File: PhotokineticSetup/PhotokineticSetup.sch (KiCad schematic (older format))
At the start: 28 parts, among them J1 Conn_01x02, J2 Serial, J3 LEDs, J4 Switches, J5 Outputs, J6 Inputs, J7 Conn_01x20, J8 Conn_01x20, Q1 2N3904, Q2 2N3904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

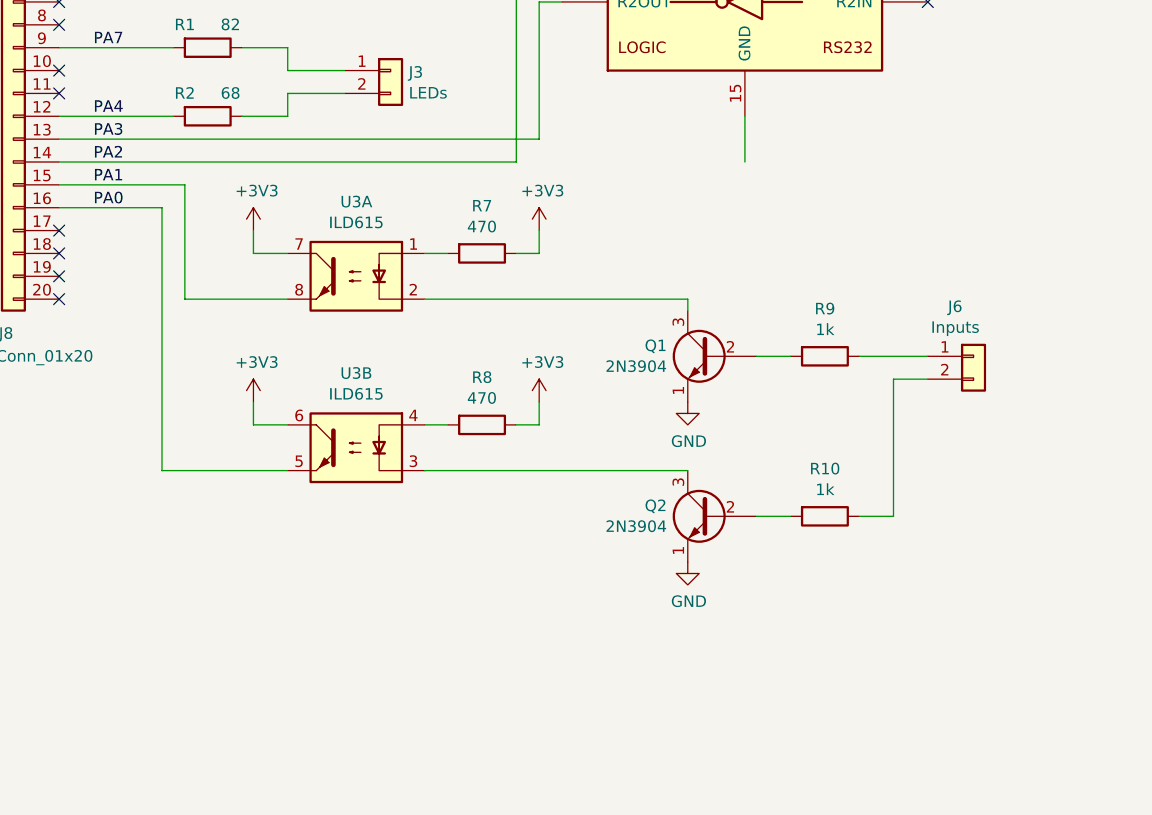
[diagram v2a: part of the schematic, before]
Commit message: Missing GND node + better placement of R7 & R8
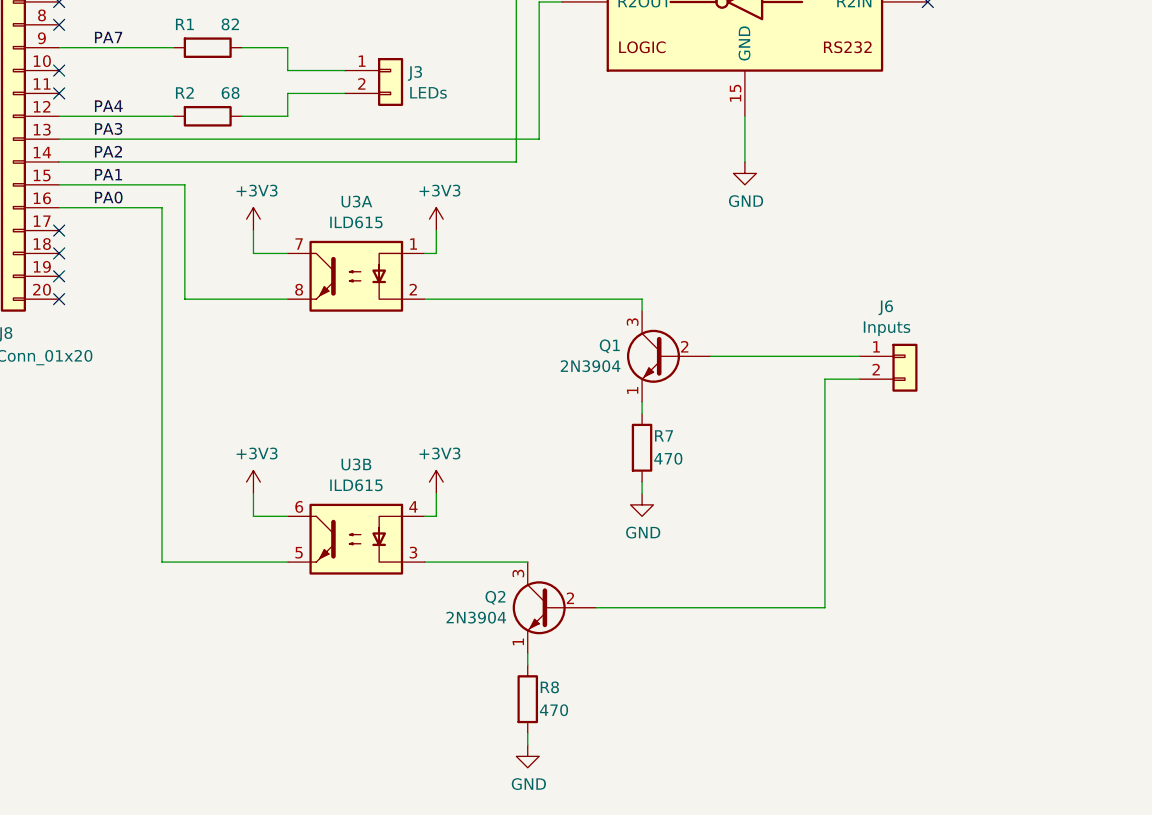
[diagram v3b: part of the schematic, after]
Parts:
- removed R10, R9: 1k, Resistor_THT:R_Axial_DIN0204_L3.6mm_D1.6mm_P7.62mm_Horizontal, symbol Device:R
- renumbered R8 to R7, R7 to R8
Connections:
- net +3V3: now also U3.1, U3.4; no longer R7.1, R8.1
- net GND: now also R7.2, R8.2, U1.15 (GND); no longer Q1.1 (E), Q2.1 (E)
- net at J6.1 (Pin_1): now also Q1.2 (B)
- net at J6.2 (Pin_2): now also Q2.2 (B)
- new net: Q1.1 (E), R7.1
- new net: Q2.1 (E), R8.1
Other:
- moved on the sheet: J6, Q1, Q2, R7, R8, U3B
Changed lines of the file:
@@
 	8250 4150 8250 4350
-$Comp
-L power:GND #PWR0104
-U 1 1 60C4DEDC
-P 8000 5400
-F 0 "#PWR0104" H 8000 5150 50  0001 C CNN
-F 1 "GND" H 8005 5227 50  0000 C CNN
-F 2 "" H 8000 5400 50  0001 C CNN
-F 3 "" H 8000 5400 50  0001 C CNN
-	1    8000 5400
-	1    0    0    -1
-$EndComp
 $Comp
 L power:+5V #PWR0105
@@
 L Connector_Generic:Conn_01x02 J6
 U 1 1 60C97537
-P 9250 5200
-F 0 "J6" H 9170 5417 50  0000 C CNN
-F 1 "Inputs" H 9170 5326 50  0000 C CNN
-F 2 "Connector_PinHeader_2.54mm:PinHeader_1x02_P2.54mm_Vertical" H 9250 5200 50  0001 C CNN
-F 3 "~" H 9250 5200 50  0001 C CNN
-	1    9250 5200
+P 8950 5200
+F 0 "J6" H 8870 5417 50  0000 C CNN
+F 1 "Inputs" H 8870 5326 50  0000 C CNN
+F 2 "Connector_PinHeader_2.54mm:PinHeader_1x02_P2.54mm_Vertical" H 8950 5200 50  0001 C CNN
+F 3 "~" H 8950 5200 50  0001 C CNN
+	1    8950 5200
 	1    0    0    -1
 $EndComp
@@
 L Isolator:ILD74 U3
 U 2 1 60CA65A1
-P 6550 5600
-F 0 "U3" H 6550 5925 50  0000 C CNN
-F 1 "ILD615" H 6550 5834 50  0000 C CNN
-F 2 "Package_DIP:DIP-8_W7.62mm_Socket_LongPads" H 6350 5400 50  0001 L CIN
-F 3 "https://www.vishay.com/docs/83640/ild74.pdf" H 6550 5600 50  0001 L CNN
-	2    6550 5600
-	-1   0    0    -1
+P 6550 6000
+F 0 "U3" H 6550 6325 50  0000 C CNN
+F 1 "ILD615" H 6550 6234 50  0000 C CNN
+F 2 "Package_DIP:DIP-8_W7.62mm_Socket_LongPads" H 6350 5800 50  0001 L CIN
+F 3 "https://www.vishay.com/docs/83640/ild74.pdf" H 6550 6000 50  0001 L CNN
+	2    6550 6000
+	-1   0    0    -1
+$EndComp
+$Comp
+L Device:R R8
+U 1 1 60CA929B
+P 7300 6700
+F 0 "R8" H 7350 6750 50  0000 L CNN
+F 1 "470" H 7350 6650 50  0000 L CNN
+F 2 "Resistor_THT:R_Axial_DIN0204_L3.6mm_D1.6mm_P7.62mm_Horizontal" V 7230 6700 50  0001 C CNN
+F 3 "~" H 7300 6700 50  0001 C CNN
+	1    7300 6700
+	1    0    0    -1
 $EndComp
 $Comp
 L Device:R R7
-U 1 1 60CA929B
-P 7100 4750
-F 0 "R7" V 6893 4750 50  0000 C CNN
-F 1 "470" V 6984 4750 50  0000 C CNN
-F 2 "Resistor_THT:R_Axial_DIN0204_L3.6mm_D1.6mm_P7.62mm_Horizontal" V 7030 4750 50  0001 C CNN
-F 3 "~" H 7100 4750 50  0001 C CNN
-	1    7100 4750
-	0    1    1    0
-$EndComp
-$Comp
-L Device:R R8
 U 1 1 60CA92A2
-P 7100 5500
-F 0 "R8" V 6893 5500 50  0000 C CNN
-F 1 "470" V 6984 5500 50  0000 C CNN
-F 2 "Resistor_THT:R_Axial_DIN0204_L3.6mm_D1.6mm_P7.62mm_Horizontal" V 7030 5500 50  0001 C CNN
-F 3 "~" H 7100 5500 50  0001 C CNN
-	1    7100 5500
-	0    1    1    0
+P 7800 5600
+F 0 "R7" H 7850 5650 50  0000 L CNN
+F 1 "470" H 7850 5550 50  0000 L CNN
+F 2 "Resistor_THT:R_Axial_DIN0204_L3.6mm_D1.6mm_P7.62mm_Horizontal" V 7730 5600 50  0001 C CNN
+F 3 "~" H 7800 5600 50  0001 C CNN
+	1    7800 5600
+	1    0    0    -1
 $EndComp
 $Sheet
@@
 L Transistor_BJT:2N3904 Q1
 U 1 1 60CA79CE
-P 8100 5200
-F 0 "Q1" H 8291 5246 50  0000 L CNN
-F 1 "2N3904" H 8291 5155 50  0000 L CNN
-F 2 "Package_TO_SOT_THT:TO-92_Inline" H 8300 5125 50  0001 L CIN
-F 3 "https://www.fairchildsemi.com/datasheets/2N/2N3904.pdf" H 8100 5200 50  0001 L CNN
-	1    8100 5200
-	-1   0    0    -1
-$EndComp
-Wire Wire Line
-	7250 4750 7350 4750
-Wire Wire Line
-	7250 5500 7350 5500
+P 7900 5200
+F 0 "Q1" H 8091 5246 50  0000 L CNN
+F 1 "2N3904" H 8091 5155 50  0000 L CNN
+F 2 "Package_TO_SOT_THT:TO-92_Inline" H 8100 5125 50  0001 L CIN
+F 3 "https://www.fairchildsemi.com/datasheets/2N/2N3904.pdf" H 7900 5200 50  0001 L CNN
+	1    7900 5200
+	-1   0    0    -1
+$EndComp
 $Comp
 L power:+3V3 #PWR0113
 U 1 1 60CFEBE2
-P 7350 4650
-F 0 "#PWR0113" H 7350 4500 50  0001 C CNN
-F 1 "+3V3" H 7365 4823 50  0000 C CNN
-F 2 "" H 7350 4650 50  0001 C CNN
-F 3 "" H 7350 4650 50  0001 C CNN
-	1    7350 4650
-	1    0    0    -1
-$EndComp
-Wire Wire Line
-	7350 4650 7350 4750
+P 6900 4650
+F 0 "#PWR0113" H 6900 4500 50  0001 C CNN
+F 1 "+3V3" H 6915 4823 50  0000 C CNN
+F 2 "" H 6900 4650 50  0001 C CNN
+F 3 "" H 6900 4650 50  0001 C CNN
+	1    6900 4650
+	1    0    0    -1
+$EndComp
+Wire Wire Line
+	6900 4650 6900 4750
 $Comp
 L power:+3V3 #PWR0114
 U 1 1 60D3CEA5
-P 7350 5400
-F 0 "#PWR0114" H 7350 5250 50  0001 C CNN
-F 1 "+3V3" H 7365 5573 50  0000 C CNN
-F 2 "" H 7350 5400 50  0001 C CNN
-F 3 "" H 7350 5400 50  0001 C CNN
-	1    7350 5400
-	1    0    0    -1
-$EndComp
-Wire Wire Line
-	7350 5400 7350 5500
-Wire Wire Line
-	6850 4750 6950 4750
-Wire Wire Line
-	6850 5500 6950 5500
-Wire Wire Line
-	8000 4950 8000 5000
-Wire Wire Line
-	6850 4950 8000 4950
+P 6900 5800
+F 0 "#PWR0114" H 6900 5650 50  0001 C CNN
+F 1 "+3V3" H 6915 5973 50  0000 C CNN
+F 2 "" H 6900 5800 50  0001 C CNN
+F 3 "" H 6900 5800 50  0001 C CNN
+	1    6900 5800
+	1    0    0    -1
+$EndComp
+Wire Wire Line
+	6900 5800 6900 5900
+Wire Wire Line
+	6850 4750 6900 4750
+Wire Wire Line
+	6850 5900 6900 5900
+Wire Wire Line
+	7800 4950 7800 5000
 $Comp
 L power:GND #PWR0115
 U 1 1 60D5D869
-P 8000 6100
-F 0 "#PWR0115" H 8000 5850 50  0001 C CNN
-F 1 "GND" H 8005 5927 50  0000 C CNN
-F 2 "" H 8000 6100 50  0001 C CNN
-F 3 "" H 8000 6100 50  0001 C CNN
-	1    8000 6100
+P 7300 6900
+F 0 "#PWR0115" H 7300 6650 50  0001 C CNN
+F 1 "GND" H 7305 6727 50  0000 C CNN
+F 2 "" H 7300 6900 50  0001 C CNN
+F 3 "" H 7300 6900 50  0001 C CNN
+	1    7300 6900
 	1    0    0    -1
 $EndComp
@@
 L Transistor_BJT:2N3904 Q2
 U 1 1 60D5D86F
-P 8100 5900
-F 0 "Q2" H 8291 5946 50  0000 L CNN
-F 1 "2N3904" H 8291 5855 50  0000 L CNN
-F 2 "Package_TO_SOT_THT:TO-92_Inline" H 8300 5825 50  0001 L CIN
-F 3 "https://www.fairchildsemi.com/datasheets/2N/2N3904.pdf" H 8100 5900 50  0001 L CNN
-	1    8100 5900
-	-1   0    0    -1
-$EndComp
-Wire Wire Line
-	6850 5700 8000 5700
+P 7400 6300
+F 0 "Q2" H 7591 6346 50  0000 L CNN
+F 1 "2N3904" H 7591 6255 50  0000 L CNN
+F 2 "Package_TO_SOT_THT:TO-92_Inline" H 7600 6225 50  0001 L CIN
+F 3 "https://www.fairchildsemi.com/datasheets/2N/2N3904.pdf" H 7400 6300 50  0001 L CNN
+	1    7400 6300
+	-1   0    0    -1
+$EndComp
 Wire Wire Line
 	1250 4550 1500 4550
@@
 Wire Wire Line
 	1800 4750 1950 4750
-$Comp
-L Device:R R10
-U 1 1 60CA7C5E
-P 8600 5900
-F 0 "R10" V 8393 5900 50  0000 C CNN
-F 1 "1k" V 8484 5900 50  0000 C CNN
-F 2 "Resistor_THT:R_Axial_DIN0204_L3.6mm_D1.6mm_P7.62mm_Horizontal" V 8530 5900 50  0001 C CNN
-F 3 "~" H 8600 5900 50  0001 C CNN
-	1    8600 5900
-	0    1    1    0
-$EndComp
-Wire Wire Line
-	8900 5900 8900 5300
-Wire Wire Line
-	8900 5300 9050 5300
-Wire Wire Line
-	8300 5900 8450 5900
-Wire Wire Line
-	8750 5900 8900 5900
-$Comp
-L Device:R R9
-U 1 1 60CC280A
-P 8600 5200
-F 0 "R9" V 8393 5200 50  0000 C CNN
-F 1 "1k" V 8484 5200 50  0000 C CNN
-F 2 "Resistor_THT:R_Axial_DIN0204_L3.6mm_D1.6mm_P7.62mm_Horizontal" V 8530 5200 50  0001 C CNN
-F 3 "~" H 8600 5200 50  0001 C CNN
-	1    8600 5200
-	0    1    1    0
-$EndComp
-Wire Wire Line
-	8750 5200 9050 5200
-Wire Wire Line
-	8300 5200 8450 5200
+Wire Wire Line
+	8600 5300 8750 5300
 Wire Wire Line
 	5800 4950 6250 4950
 Wire Wire Line
-	5700 5700 6250 5700
-Wire Wire Line
-	5700 4550 5700 5700
+	5700 6100 6250 6100
 Wire Wire Line
 	5800 4450 5800 4950
@@
 L power:+3V3 #PWR?
 U 1 1 60CBE08A
-P 6100 5400
-F 0 "#PWR?" H 6100 5250 50  0001 C CNN
-F 1 "+3V3" H 6115 5573 50  0000 C CNN
-F 2 "" H 6100 5400 50  0001 C CNN
-F 3 "" H 6100 5400 50  0001 C CNN
-	1    6100 5400
-	1    0    0    -1
-$EndComp
-Wire Wire Line
-	6100 5400 6100 5500
-Wire Wire Line
-	6100 5500 6250 5500
+P 6100 5800
+F 0 "#PWR?" H 6100 5650 50  0001 C CNN
+F 1 "+3V3" H 6115 5973 50  0000 C CNN
+F 2 "" H 6100 5800 50  0001 C CNN
+F 3 "" H 6100 5800 50  0001 C CNN
+	1    6100 5800
+	1    0    0    -1
+$EndComp
+Wire Wire Line
+	6100 5800 6100 5900
+Wire Wire Line
+	6100 5900 6250 5900
+$Comp
+L power:GND #PWR?
+U 1 1 60D05AB9
+P 8250 4350
+F 0 "#PWR?" H 8250 4100 50  0001 C CNN
+F 1 "GND" H 8255 4177 50  0000 C CNN
+F 2 "" H 8250 4350 50  0001 C CNN
+F 3 "" H 8250 4350 50  0001 C CNN
+	1    8250 4350
+	1    0    0    -1
+$EndComp
+Wire Wire Line
+	5700 4550 5700 6100
+Wire Wire Line
+	8100 5200 8750 5200
+Wire Wire Line
+	7600 6300 8600 6300
+$Comp
+L power:GND #PWR?
+U 1 1 60D74D00
+P 7800 5800
+F 0 "#PWR?" H 7800 5550 50  0001 C CNN
+F 1 "GND" H 7805 5627 50  0000 C CNN
+F 2 "" H 7800 5800 50  0001 C CNN
+F 3 "" H 7800 5800 50  0001 C CNN
+	1    7800 5800
+	1    0    0    -1
+$EndComp
+Wire Wire Line
+	7800 5750 7800 5800
+Wire Wire Line
+	7800 5400 7800 5450
+Wire Wire Line
+	8600 5300 8600 6300
+Wire Wire Line
+	6850 6100 7300 6100
+Wire Wire Line
+	6850 4950 7800 4950
+Wire Wire Line
+	7300 6850 7300 6900
+Wire Wire Line
+	7300 6500 7300 6550
 $EndSCHEMATC
